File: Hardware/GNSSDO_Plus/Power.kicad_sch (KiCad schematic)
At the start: 44 parts, among them U11 AP7361C-3.3V, U18 LM66200, U21 LM66200, U22 LM66200, U5 AP7361C-3.3V, U6 REC15E-2405SZ, U7 Ag9205-S

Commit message: GNSSDO+ WIP
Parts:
- added C89, C90: 1.0uF, SparkFun-Capacitor:C_0603_1608Metric, symbol SparkFun-Capacitor:1.0uF_0603_16V_10%
- added TP29: PTH, SparkFun-Connector:1x01, symbol SparkFun-Connector:TestPoint_PTH
- added U25: AP2112K-3.3, SparkFun-Semiconductor-Standard:SOT23-5, symbol SparkFun-Regulator:AP2112K-3.3
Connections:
- net GND: now also C89.2, C90.2, U25.2 (GND)
- net VBUS: now also C89.1, U25.1 (VIN), U25.3 (EN)
- new net 3.3V_A: C90.1, TP29.1, U25.5 (VOUT)
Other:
- note added: "Analog 3.3V"

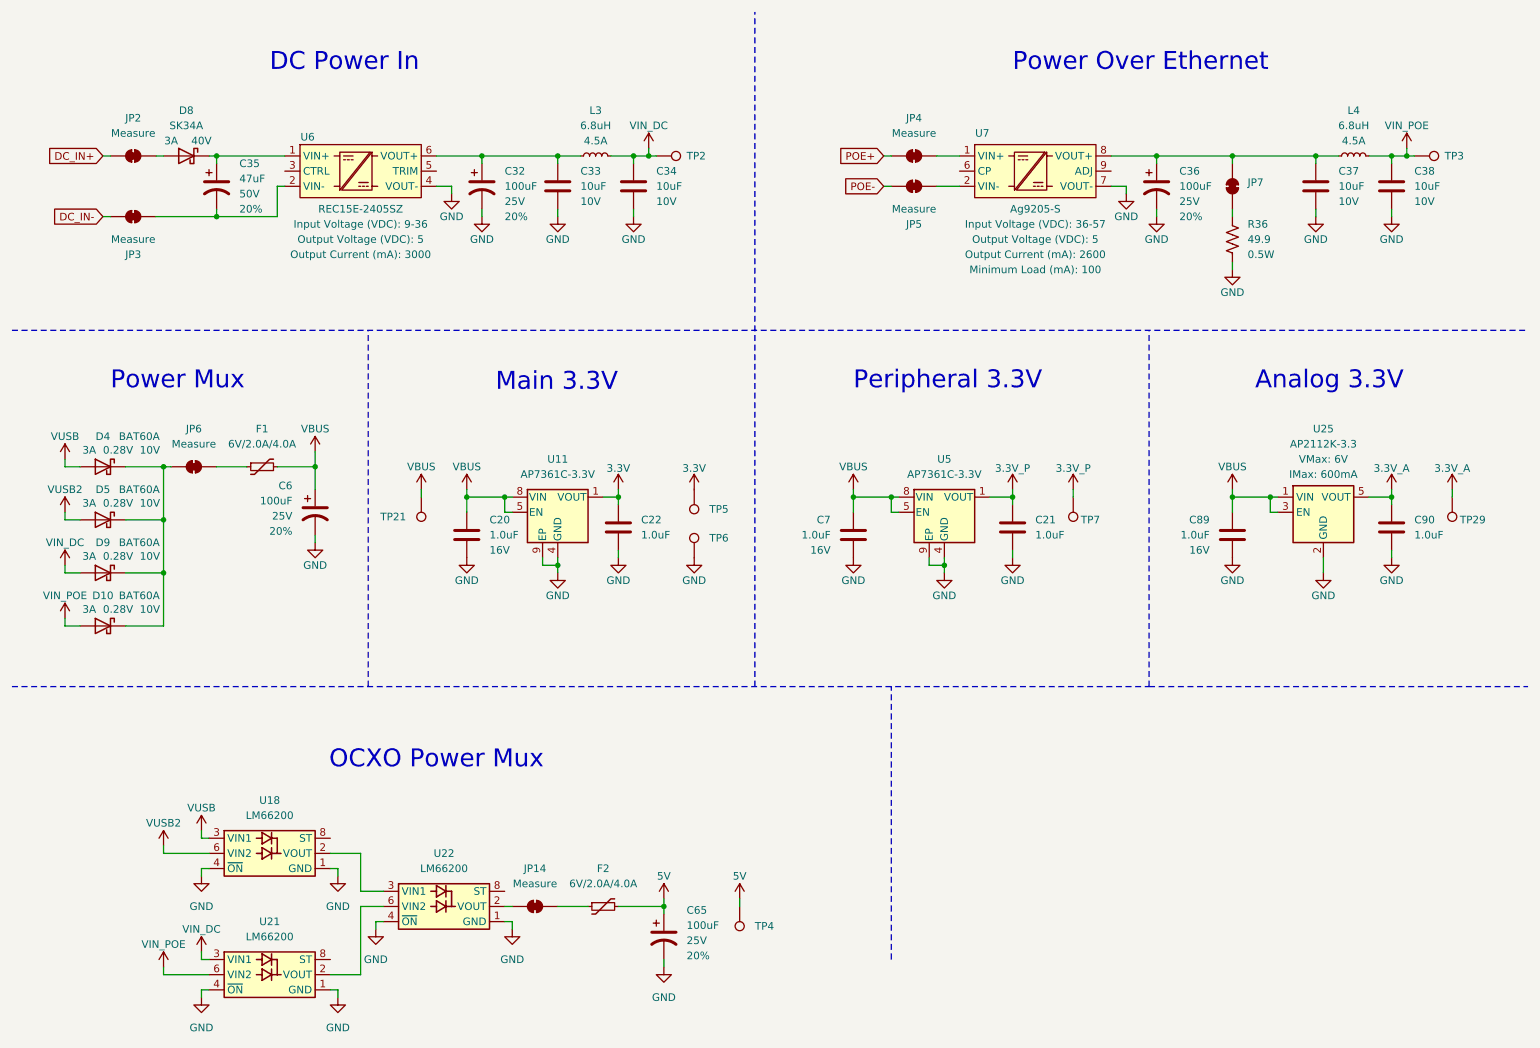
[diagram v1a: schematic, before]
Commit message: GNSSDO+ : update symbols and footprints
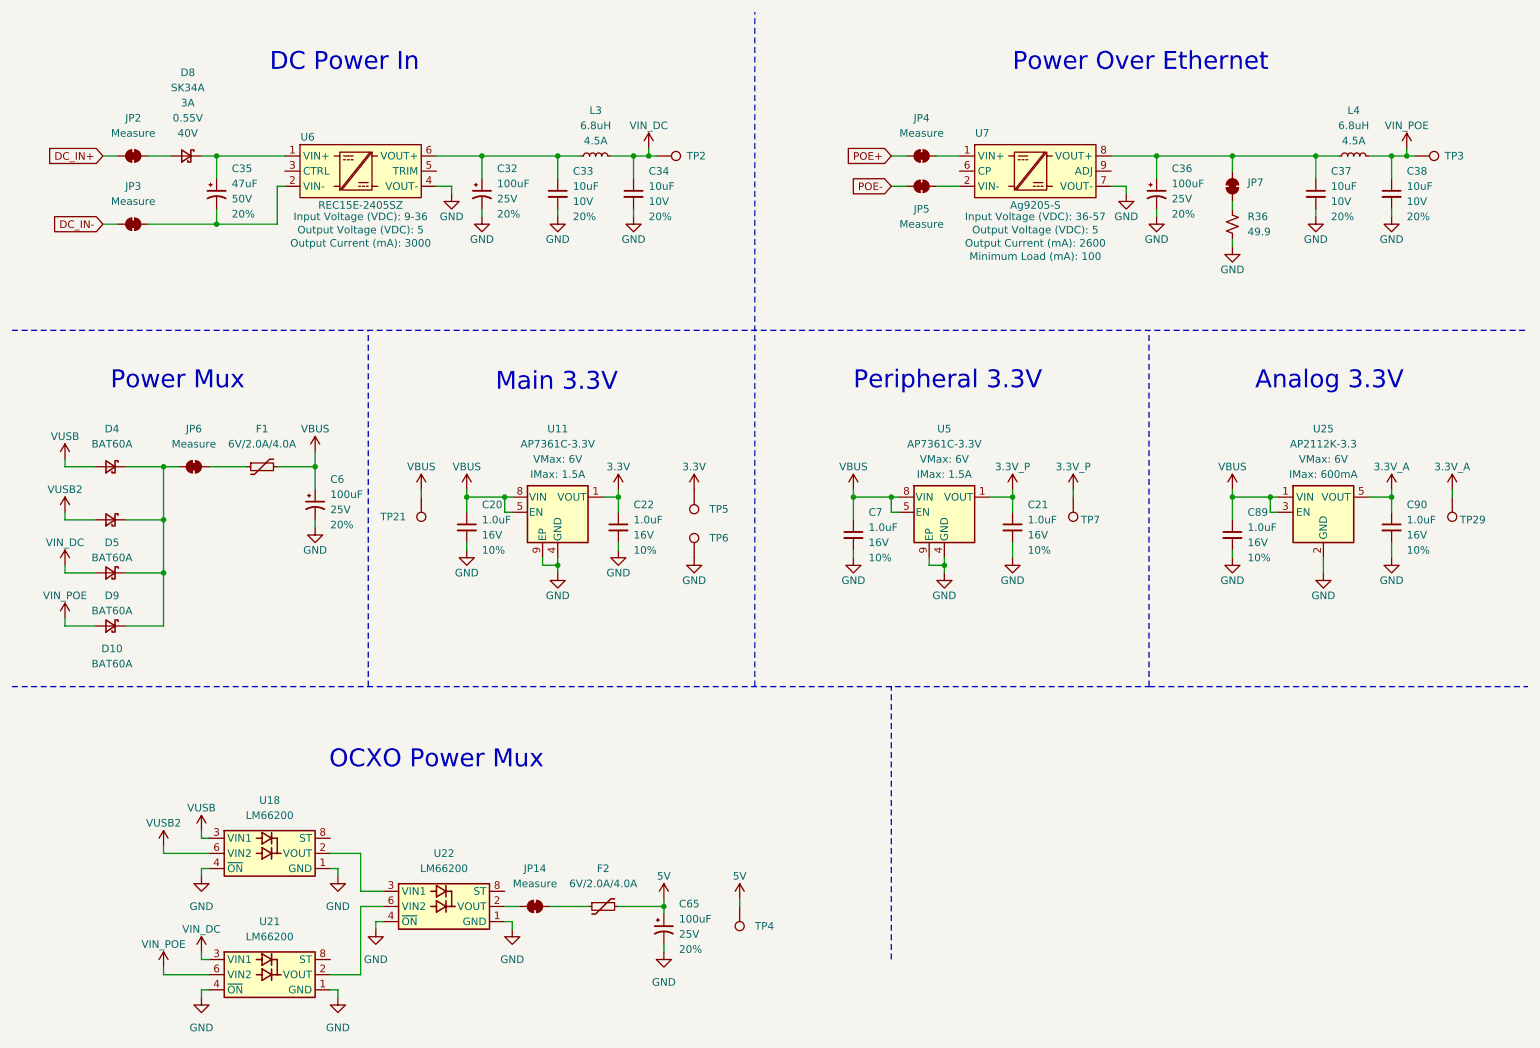
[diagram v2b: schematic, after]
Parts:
- U11, U5: IMax (none) -> 1.5A; Imax 1.5A -> (none)
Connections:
- net GND: now also R36.2; no longer R36.1
- net VIN_DC: now also D9.2 (A); no longer D9.A
- net VIN_POE: now also D10.2 (A); no longer D10.A
- net VUSB: now also D4.2 (A); no longer D4.A
- net VUSB2: now also D5.2 (A); no longer D5.A
- net at C35.1, U6.1 (VIN+): now also D8.1 (K); no longer D8.C
- net at JP2.2 (B): now also D8.2 (A); no longer D8.A
- net at JP7.1 (A): now also R36.1; no longer R36.2
- new net: D10.1 (K), D4.1 (K), D5.1 (K), D9.1 (K), JP6.1 (A)
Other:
- moved on the sheet: C20, C32, C33, C34, C35, C36, C37, C38, C6, C65, D10, D4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

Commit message: GNSSDO Plus - ready for review
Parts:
- added TP1: PTH, SparkFun-Connector:1x01, symbol SparkFun-Connector:TestPoint_PTH
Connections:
- net GND: now also TP1.1
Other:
- moved on the sheet: C21, C22, C35, C6, C89, C90, D8, F1, JP2, JP3, JP6, U11

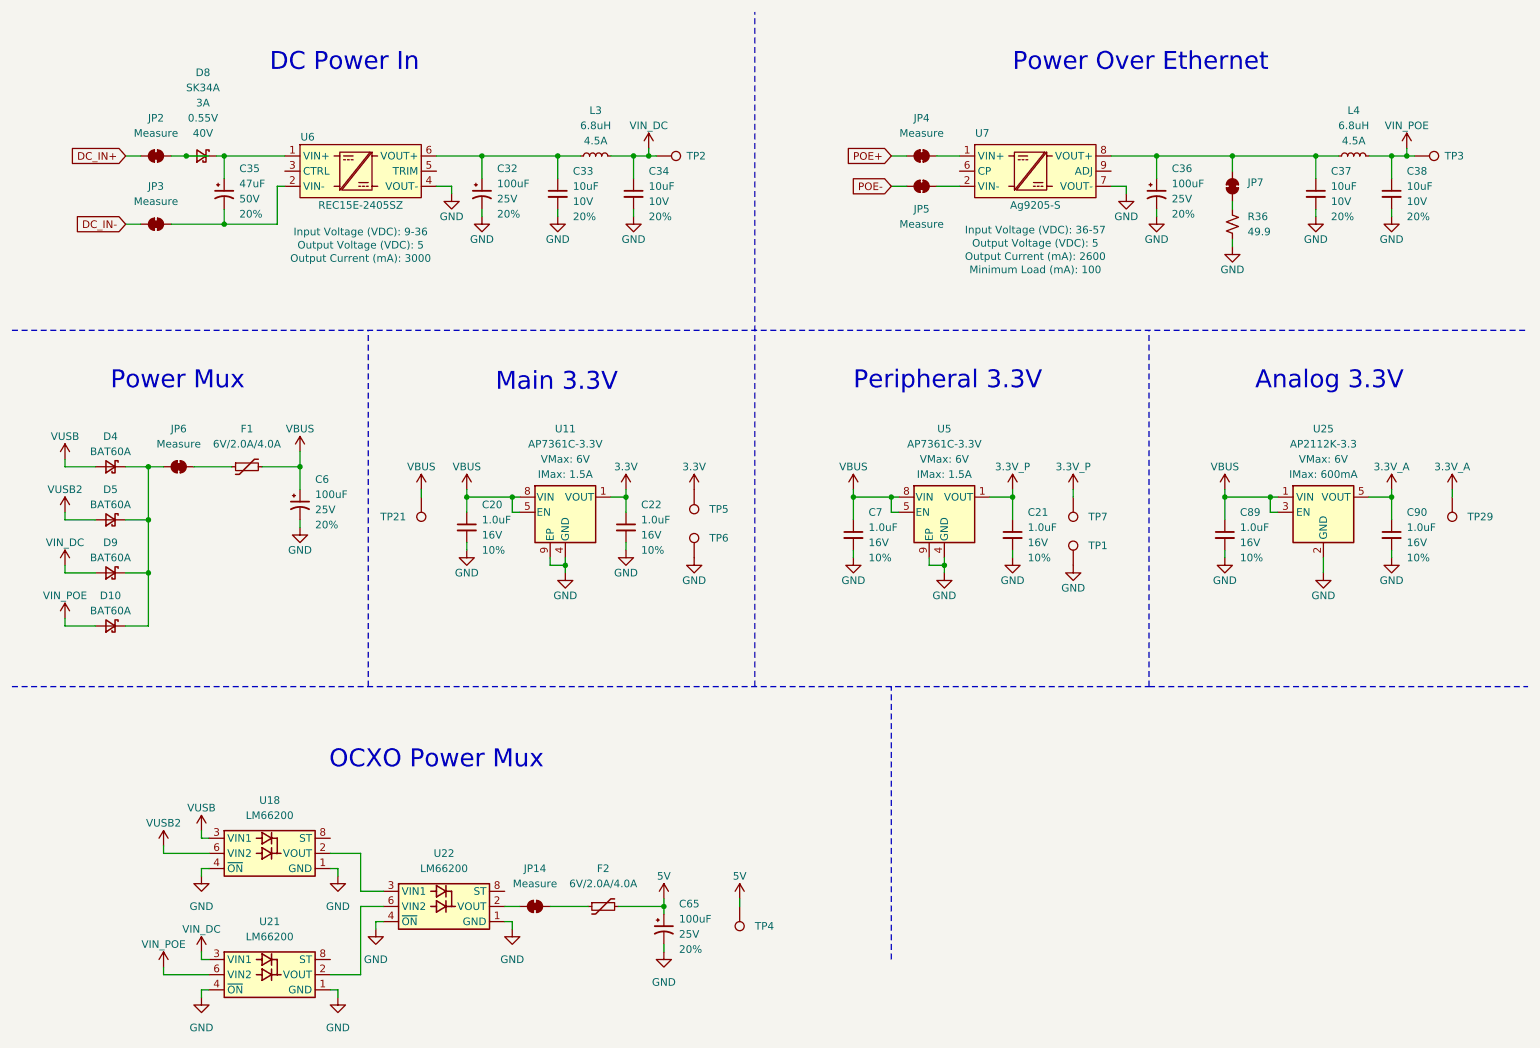
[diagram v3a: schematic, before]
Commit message: GNSSDO+ v02 PCB - with DP5305 PoE module, PowerPath Controllers and MS8607 PHT sensor
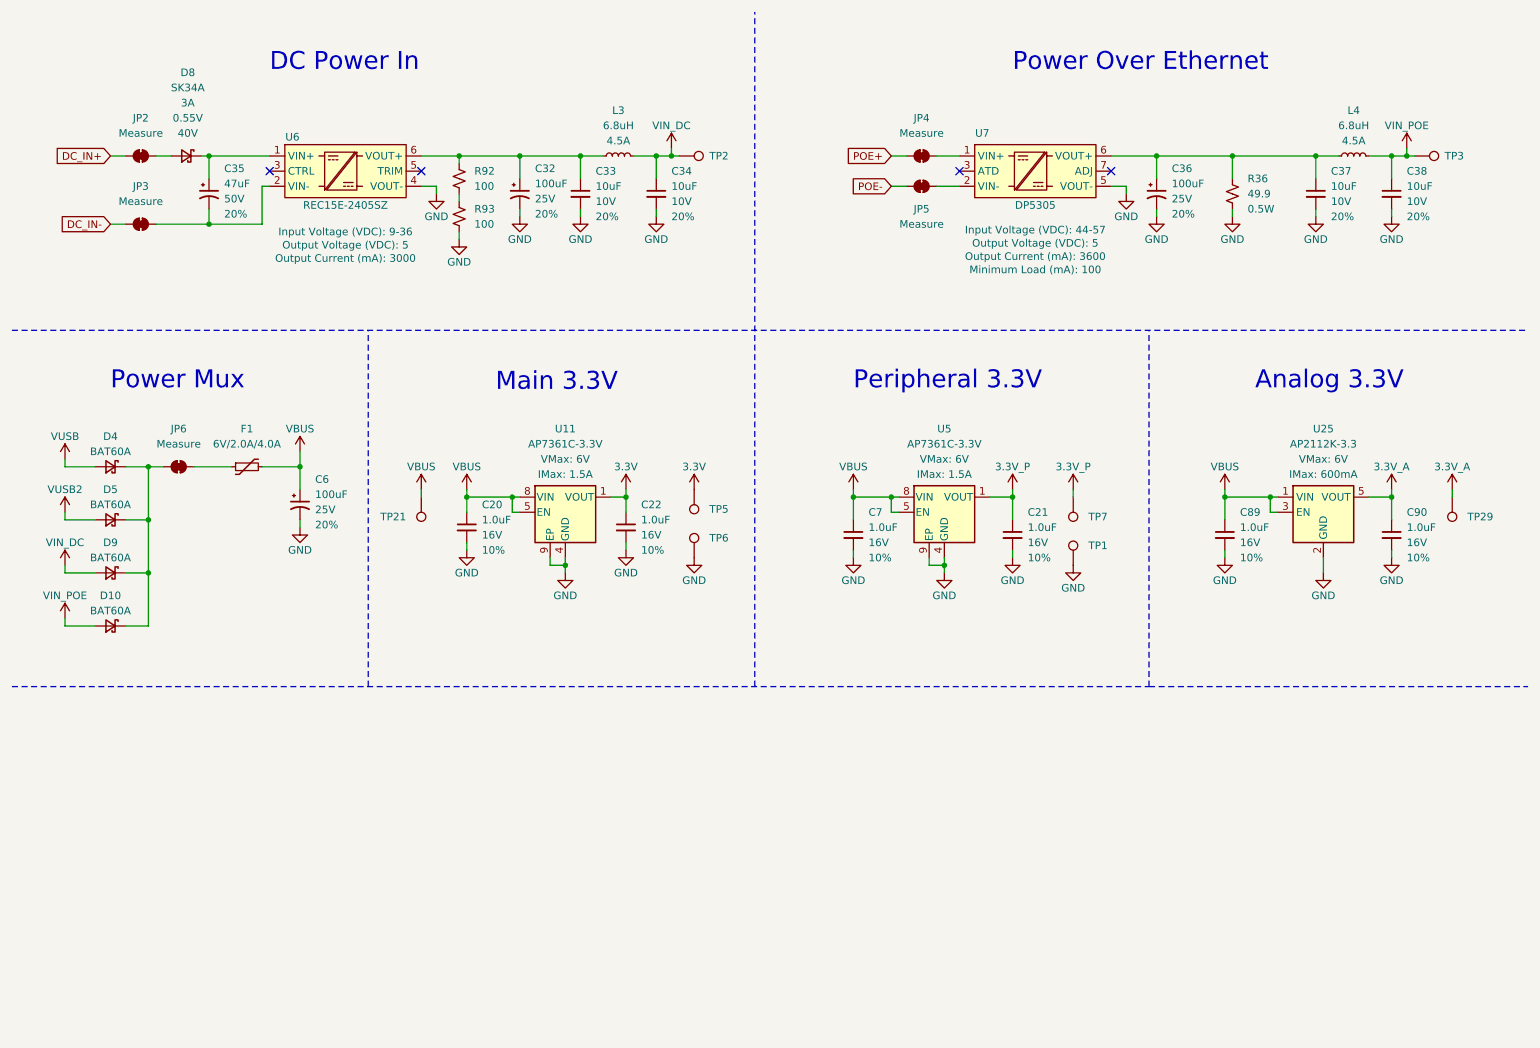
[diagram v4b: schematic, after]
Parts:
- removed C65: 100uF, SparkFun-Capacitor:Panasonic_D, symbol SparkFun-Capacitor:100uF_6.6x6.6_25V_20%
- removed F2: 6V/2.0A/4.0A, SparkFun-Fuse:1210, symbol SparkFun-Fuse:Fuse 6V/2.0A/4.0A
- removed JP14: Measure, SparkFun-Jumper:Jumper_2_PTH_SMD_Combo-NC, symbol SparkFun-Jumper:Jumper_Measure
- removed JP7: ~, SparkFun-Jumper:Jumper_2_NC_Trace, symbol SparkFun-Jumper:SolderJumper_2_Bridged
- removed TP4: PTH, SparkFun-Connector:1x01, symbol SparkFun-Connector:TestPoint_PTH
- removed U18, U21, U22: LM66200, SparkFun-Semiconductor-Standard:SOT-583-8, symbol SparkFun-IC-Power:LM66200_(Small)
- added R92, R93: 100, SparkFun-Resistor:R_0603_1608Metric, symbol SparkFun-Resistor:100_0603
- U11, U5: footprint SparkFun-Semiconductor-Standard:UDFN-8 -> SparkFun-Semiconductor-Standard:DFN-8_3x3mm_P0.65mm_EP2.25x1.5mm
- U7: value Ag9205-S -> DP5305; footprint SparkFun-Semiconductor-Nonstandard:Ag9200 -> SparkFun-Semiconductor-Nonstandard:DP5300; symbol SparkFun-IC-Power:Ag9205-S -> SparkFun-IC-Power:DP5305; Input Voltage (VDC) 36-57 -> 44-57; Output Current (mA) 2600 -> 3600; PROD_ID IC-24774 -> IC-26655
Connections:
- net GND: now also U7.5 (VOUT-), U7.8 (VOUT-), R93.1; no longer U7.7 (VOUT-)
- net at C32.1, C33.1, L3.1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: now also R92.2
- net at C36.1, C37.1, L4.1: now also R36.1, U7.6 (VOUT+); no longer U7.8 (VOUT+)
- net VIN+: no longer names the net of JP4.2 (B), U7.1 (VIN+)
- net VIN+: no longer U7.3 (VIN+)
- net VIN-: no longer names the net of JP5.2 (B), U7.2 (VIN-)
- net VIN-: no longer U7.4 (VIN-), U7.5 (VIN-)
- new net: R92.1, R93.2
- now unconnected: U11.2 (NC), U11.3 (NC), U11.6 (NC), U11.7 (NC), U5.2 (NC), U5.3 (NC), U5.6 (NC), U5.7 (NC)
- no-connect marks 0 -> 4
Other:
- note removed: "OCXO Power Mux"
- title: Power -> GNSSDO Plus - Power
- moved on the sheet: C32, C33, C34, C35, D8, JP2, JP3, L3, R36, TP2, U6

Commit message: Update GNSSDO KiCad files to match latest SparkFun library
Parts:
- TP1, TP2, TP21, TP29, TP3, TP5, TP6, TP7: footprint SparkFun-Connector:1x01 -> SparkFun-Connector:1x01_P2.54mm
